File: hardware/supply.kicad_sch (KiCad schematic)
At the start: 27 parts, among them U11 LMR38010SDDAR, U7 LM1117-3.3

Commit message: changed pcb version
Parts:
- added C23: 100nF, Capacitor_SMD:C_0201_0603Metric_Pad0.64x0.40mm_HandSolder, symbol Device:C
- added C27, C28: 100nF, Capacitor_SMD:C_0603_1608Metric_Pad1.08x0.95mm_HandSolder, symbol Device:C
- added D10: BZX38450-C3V3-QX, Diode_SMD:D_SOD-323_HandSoldering, symbol Device:D_Zener
- added R25: 2.2k, Resistor_SMD:R_0603_1608Metric_Pad0.98x0.95mm_HandSolder, symbol Device:R
- added U2: 4011, Package_SO:TSSOP-14_4.4x5mm_P0.65mm, symbol 4xxx:4011
- added U3: 4081, Package_SO:TSSOP-14_4.4x5mm_P0.65mm, symbol 4xxx:4081
- added U4: 4071, Package_SO:TSSOP-14_4.4x5mm_P0.65mm, symbol 4xxx:4071
- Cboot1: footprint Capacitor_SMD:C_0603_1608Metric -> Capacitor_SMD:C_0402_1005Metric_Pad0.74x0.62mm_HandSolder
- Rfbb1: value 3k 1% low T coeff -> 2,43k; footprint Resistor_SMD:R_0603_1608Metric -> Resistor_SMD:R_0402_1005Metric_Pad0.72x0.64mm_HandSolder
- Rfbt1: value 12k 1% low T coeff -> 9,76k; footprint Resistor_SMD:R_0603_1608Metric -> Resistor_SMD:R_0402_1005Metric_Pad0.72x0.64mm_HandSolder
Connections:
- net +3V3: now also C23.1, C27.1, C28.1, R25.1, U2.14 (VDD), U3.14 (VDD), U4.14 (VDD)
- net GND: now also C23.2, C27.2, C28.2, D10.2 (A), U2.7 (VSS), U3.7 (VSS), U4.7 (VSS)
- new net: D10.1 (K), R25.2
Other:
- note added: "Logic IC's supply"
- moved on the sheet: Cout1, D11, R18

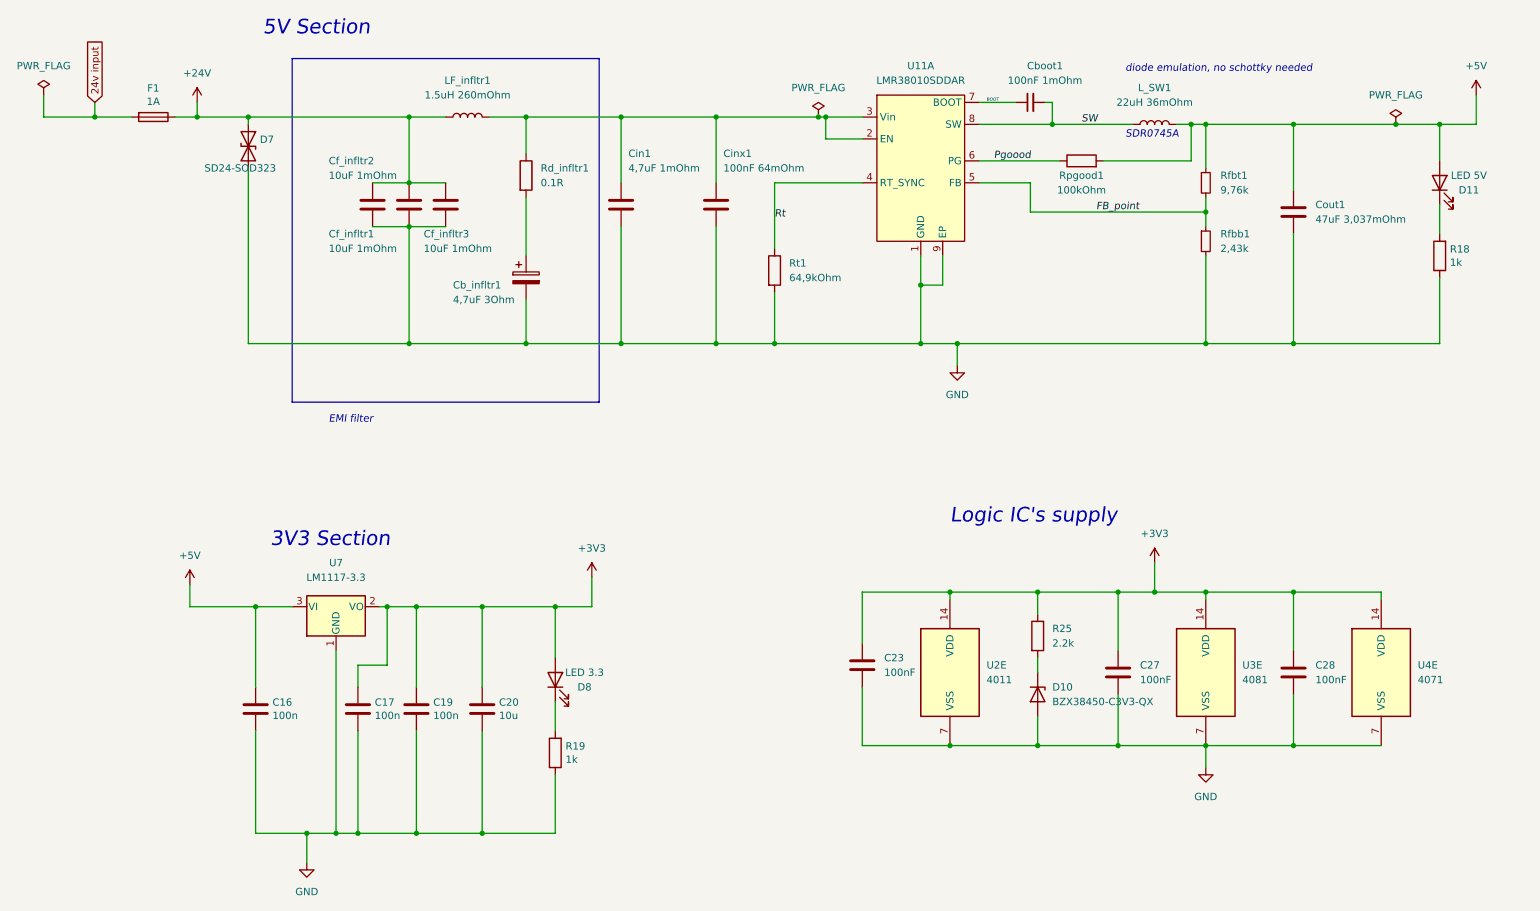
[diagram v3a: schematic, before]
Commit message: Schematic redesign for 23 rules, new pressure buffer, protection fix
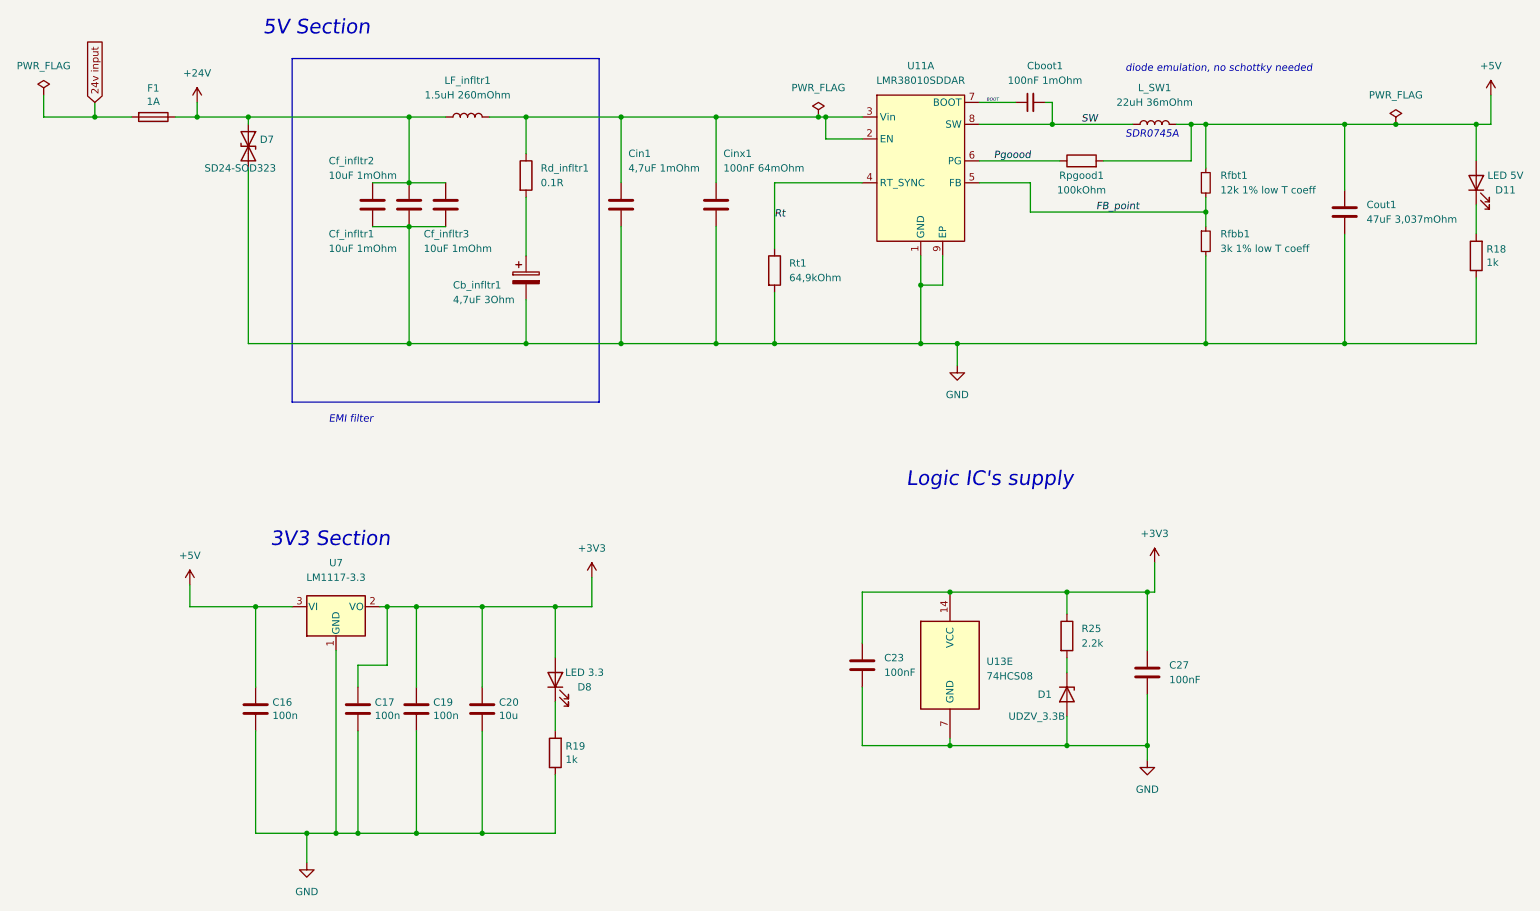
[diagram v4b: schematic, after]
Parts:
- removed C28: 100nF, Capacitor_SMD:C_0603_1608Metric_Pad1.08x0.95mm_HandSolder, symbol Device:C
- removed D10: BZX38450-C3V3-QX, Diode_SMD:D_SOD-323_HandSoldering, symbol Device:D_Zener
- removed U2: 4011, Package_SO:TSSOP-14_4.4x5mm_P0.65mm, symbol 4xxx:4011
- removed U3: 4081, Package_SO:TSSOP-14_4.4x5mm_P0.65mm, symbol 4xxx:4081
- removed U4: 4071, Package_SO:TSSOP-14_4.4x5mm_P0.65mm, symbol 4xxx:4071
- added D1: UDZV_3.3B, Diode_SMD:D_SOD-323_HandSoldering, symbol Device:D_Zener
- added U13: 74HCS08, Package_SO:SOIC-14_3.9x8.7mm_P1.27mm, symbol 74xx:74LS08
- Rfbb1: value 2,43k -> 3k 1% low T coeff
- Rfbt1: value 9,76k -> 12k 1% low T coeff
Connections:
- net +3V3: now also U13.14 (VCC)
- net GND: now also D1.2 (A), U13.7 (GND)
- net at R25.2: now also D1.1 (K)
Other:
- moved on the sheet: C27, Cout1, D11, R18, R25

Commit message: WIP revision 2 layout refinement
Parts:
- removed C23: 100nF, Capacitor_SMD:C_0201_0603Metric_Pad0.64x0.40mm_HandSolder, symbol Device:C
- removed C27: 100nF, Capacitor_SMD:C_0603_1608Metric_Pad1.08x0.95mm_HandSolder, symbol Device:C
- removed D1: UDZV_3.3B, Diode_SMD:D_SOD-323_HandSoldering, symbol Device:D_Zener
- removed R25: 2.2k, Resistor_SMD:R_0603_1608Metric_Pad0.98x0.95mm_HandSolder, symbol Device:R
- removed U13: 74HCS08, Package_SO:SOIC-14_3.9x8.7mm_P1.27mm, symbol 74xx:74LS08
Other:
- note removed: "Logic IC's supply"

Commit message: 2.0 layot wip , routing 2
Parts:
- Cboot1: footprint Capacitor_SMD:C_0402_1005Metric_Pad0.74x0.62mm_HandSolder -> Capacitor_SMD:C_0603_1608Metric
- Rfbb1, Rfbt1: footprint Resistor_SMD:R_0402_1005Metric_Pad0.72x0.64mm_HandSolder -> Resistor_SMD:R_0603_1608Metric
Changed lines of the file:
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@@
       (effects (font (size 1.27 1.27)) (justify left))
     )
-    (property "Footprint" "Resistor_SMD:R_0402_1005Metric_Pad0.72x0.64mm_HandSolder" (at 224.79 46.99 0)
+    (property "Footprint" "Resistor_SMD:R_0603_1608Metric" (at 224.79 46.99 0)
       (effects (font (size 1.27 1.27)) hide)
     )
@@
       (effects (font (size 1.27 1.27)) (justify left))
     )
-    (property "Footprint" "Resistor_SMD:R_0402_1005Metric_Pad0.72x0.64mm_HandSolder" (at 224.79 57.15 0)
+    (property "Footprint" "Resistor_SMD:R_0603_1608Metric" (at 224.79 57.15 0)
       (effects (font (size 1.27 1.27)) hide)
     )
@@
       (effects (font (size 1.27 1.27)))
     )
-    (property "Footprint" "Capacitor_SMD:C_0402_1005Metric_Pad0.74x0.62mm_HandSolder" (at 194.31 33.02 0)
-      (effects (font (size 1.27 1.27)) hide)
-    )
+    (property "Footprint" "Capacitor_SMD:C_0603_1608Metric" (at 194.31 33.02 0)
+      (effects (font (size 1.27 1.27)) hide)
+    )
